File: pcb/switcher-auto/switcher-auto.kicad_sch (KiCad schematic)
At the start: 24 parts, among them J0 MD-90SM, J5 Conn_02x22_Top_Bottom, SW1 SW_Push, SW2 SW_Push, U1 CD74HC4067SM96, U2 CD74HC4067SM96, U3 CD74HC4067SM96, U4 CD74HC4067SM96, U5 CD74HC4067SM96, U6 CD74HC4067SM96, U7 CD74HC4067SM96

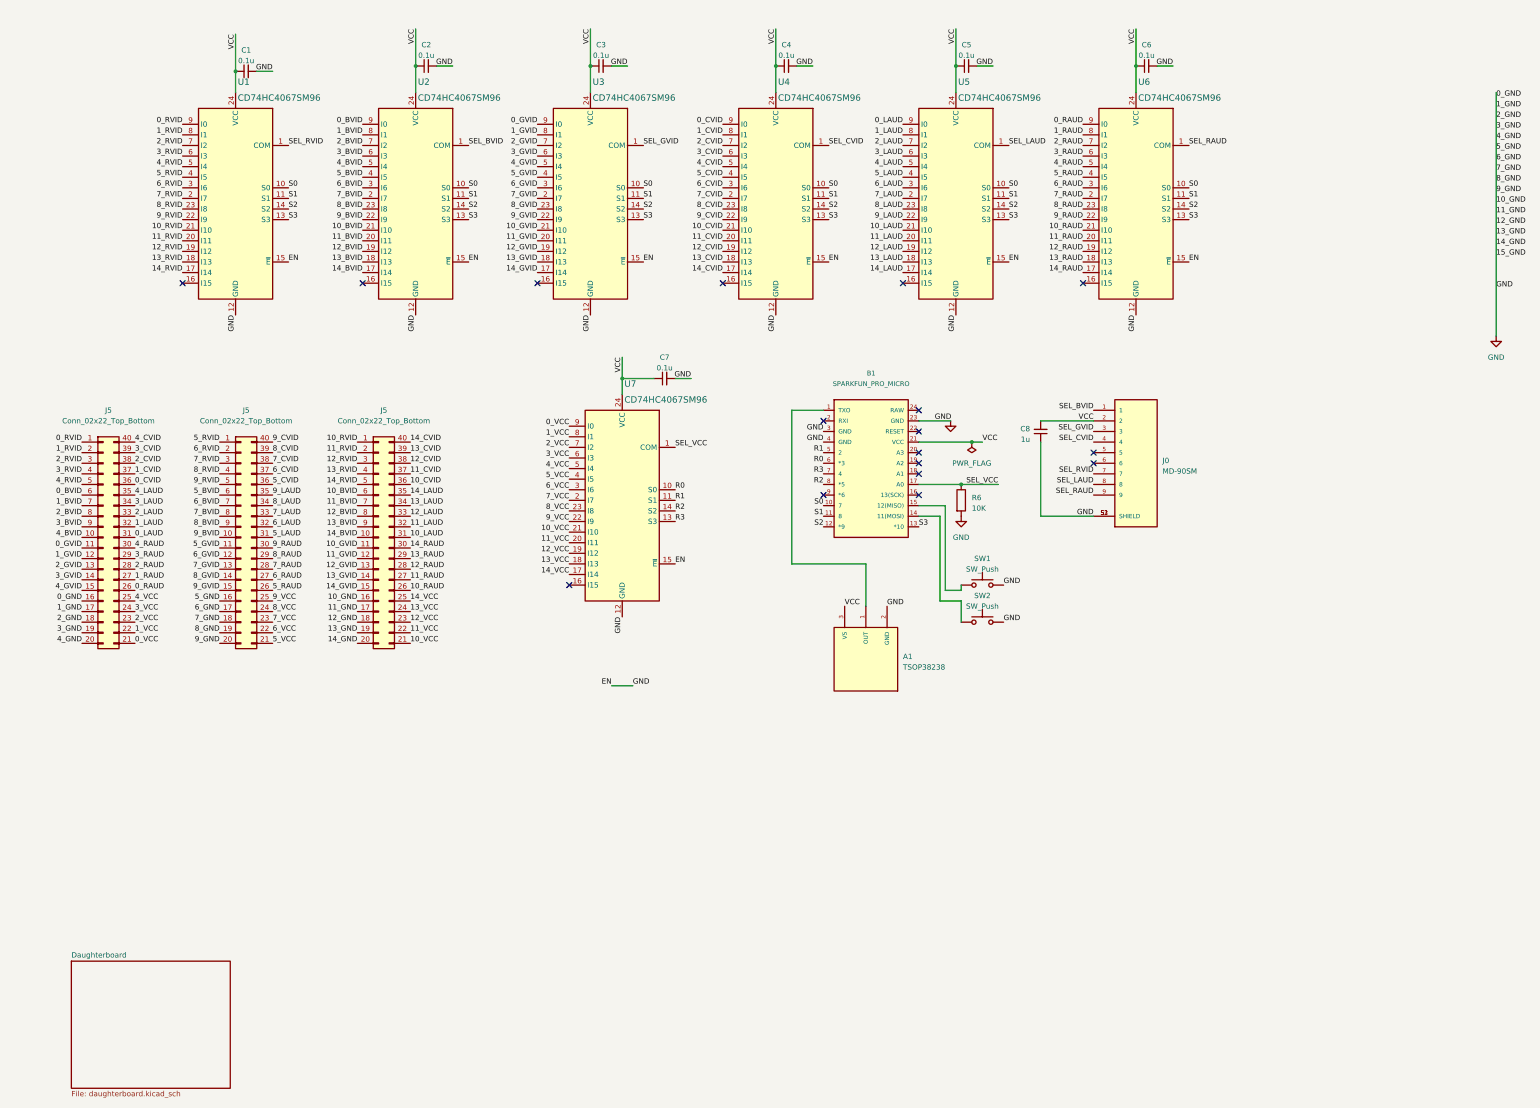
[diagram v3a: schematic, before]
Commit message: Adds THS7374 video amp
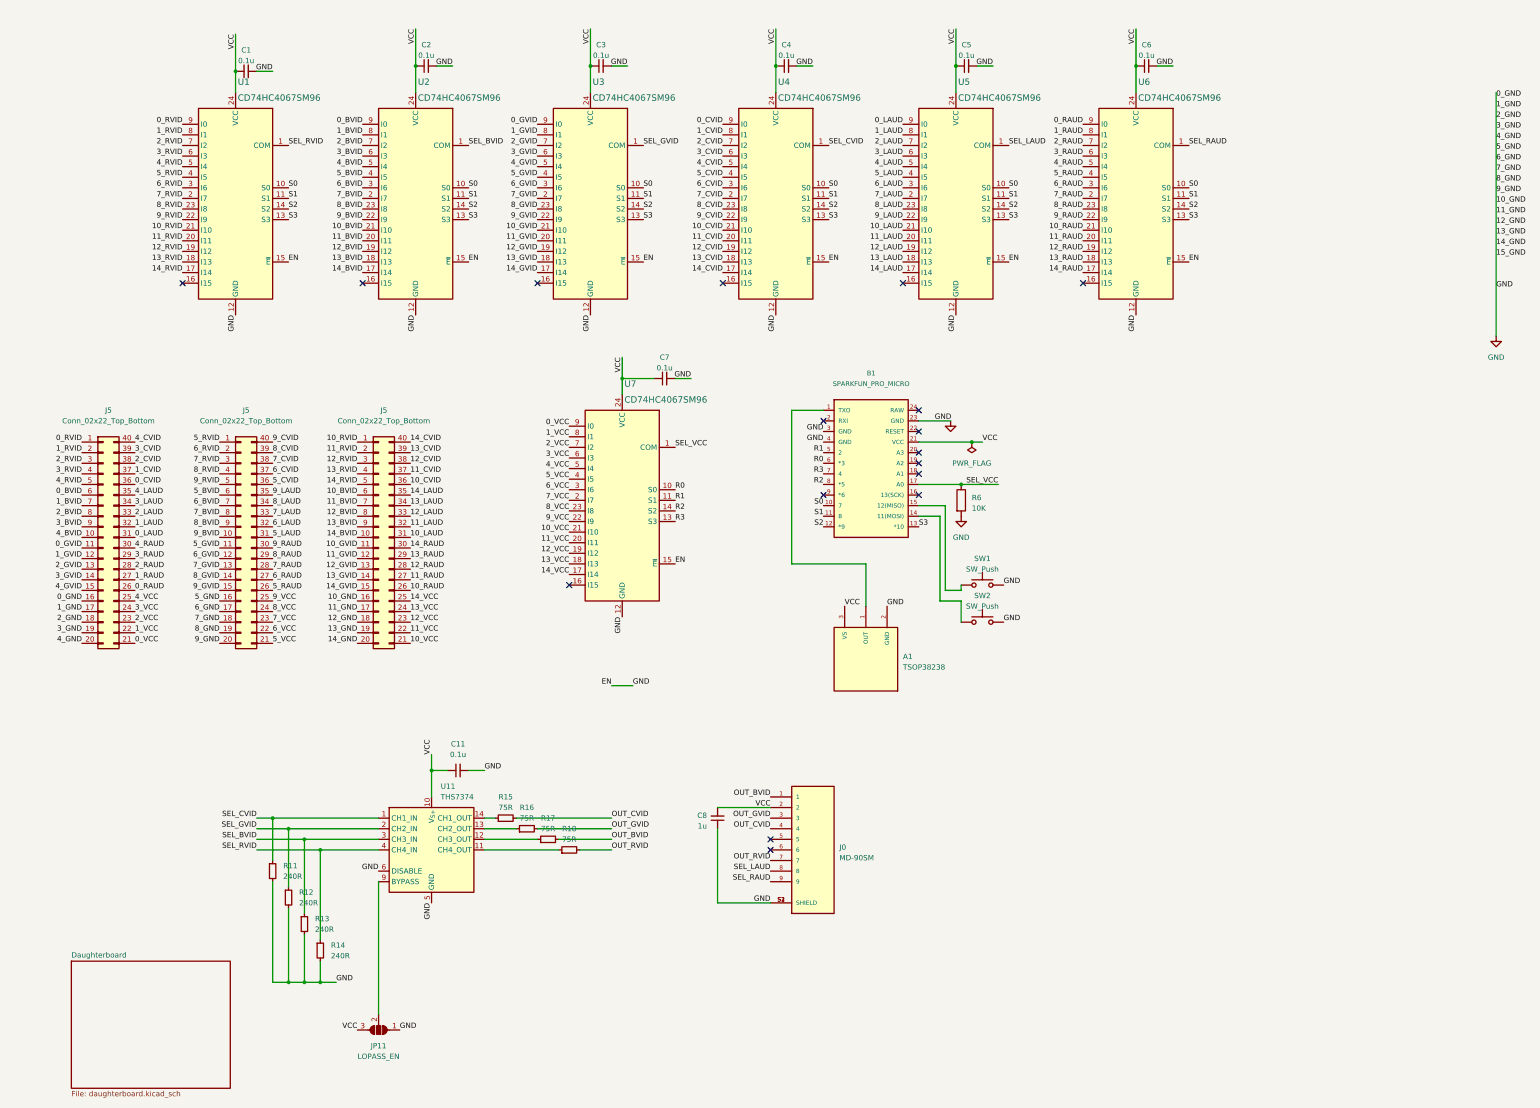
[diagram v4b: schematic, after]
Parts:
- added C11: 0.1u, Capacitor_SMD:C_0805_2012Metric_Pad1.18x1.45mm_HandSolder, symbol Device:C_Small
- added JP11: LOPASS_EN, Jumper:SolderJumper-3_P1.3mm_Open_RoundedPad1.0x1.5mm_NumberLabels, symbol Jumper:SolderJumper_3_Open
- added R11, R12, R13, R14: 240R, Resistor_SMD:R_0805_2012Metric_Pad1.20x1.40mm_HandSolder, symbol Device:R_Small
- added R15, R16, R17, R18: 75R, Resistor_SMD:R_0805_2012Metric_Pad1.20x1.40mm_HandSolder, symbol Device:R_Small
- added U11: THS7374, Package_SO:TSSOP-14_4.4x5mm_P0.65mm, symbol Amplifier_Video:THS7374
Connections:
- net GND: now also C11.2, JP11.1 (A), R11.2, R12.2, R13.2, R14.2, U11.5 (GND), U11.6 (DISABLE)
- net SEL_BVID: now also R13.1, U11.3 (CH3_IN); no longer J0.1
- net SEL_CVID: now also R11.1, U11.1 (CH1_IN); no longer J0.4
- net SEL_GVID: now also R12.1, U11.2 (CH2_IN); no longer J0.3
- net SEL_RVID: now also R14.1, U11.4 (CH4_IN); no longer J0.7
- net VCC: now also C11.1, JP11.3 (B), U11.10 (V_{S+})
- new net: R18.1, U11.11 (CH4_OUT)
- new net: R17.1, U11.12 (CH3_OUT)
- new net: R16.1, U11.13 (CH2_OUT)
- new net: R15.1, U11.14 (CH1_OUT)
- new net: JP11.2 (C), U11.9 (BYPASS)
- new net OUT_BVID: J0.1, R17.2
- new net OUT_CVID: J0.4, R15.2
- new net OUT_GVID: J0.3, R16.2
- new net OUT_RVID: J0.7, R18.2
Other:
- moved on the sheet: C8, J0

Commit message: Twiddles
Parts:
- added C12: C_Small, Capacitor_SMD:C_0805_2012Metric_Pad1.18x1.45mm_HandSolder, symbol Device:C_Small
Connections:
- net GND: now also C12.2
- net VCC: now also C12.1
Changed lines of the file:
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@@
   (junction (at 78.74 209.55) (diameter 0) (color 0 0 0 0)
   )
+  (junction (at 259.08 116.84) (diameter 0) (color 0 0 0 0)
+  )
   (junction (at 82.55 246.38) (diameter 0) (color 0 0 0 0)
   )
   (junction (at 238.76 26.67) (diameter 0) (color 0 0 0 0)
   )
-  (junction (at 242.57 116.84) (diameter 0) (color 0 0 0 0)
-  )
   (junction (at 86.36 246.38) (diameter 0) (color 0 0 0 0)
   )
@@
   (junction (at 86.36 214.63) (diameter 0) (color 0 0 0 0)
   )
+  (junction (at 248.92 116.84) (diameter 0) (color 0 0 0 0)
+  )
   (junction (at 113.03 195.58) (diameter 0) (color 0 0 0 0)
   )
@@
   )
   (junction (at 78.74 246.38) (diameter 0) (color 0 0 0 0)
-  )
-  (junction (at 240.03 127) (diameter 0) (color 0 0 0 0)
   )
   (junction (at 82.55 212.09) (diameter 0) (color 0 0 0 0)
@@
     (stroke (width 0) (type default))
   )
-  (wire (pts (xy 242.57 116.84) (xy 245.11 116.84))
-    (stroke (width 0) (type default))
-  )
   (wire (pts (xy 113.03 195.58) (xy 113.03 201.93))
     (stroke (width 0) (type default))
@@
     (stroke (width 0) (type default))
   )
+  (wire (pts (xy 248.92 116.84) (xy 259.08 116.84))
+    (stroke (width 0) (type default))
+  )
   (wire (pts (xy 71.12 209.55) (xy 78.74 209.55))
     (stroke (width 0) (type default))
@@
     (stroke (width 0) (type default))
   )
-  (wire (pts (xy 240.03 127) (xy 248.92 127))
-    (stroke (width 0) (type default))
-  )
   (wire (pts (xy 234.95 134.62) (xy 229.87 134.62))
     (stroke (width 0) (type default))
@@
     (stroke (width 0) (type default))
   )
-  (wire (pts (xy 229.87 116.84) (xy 242.57 116.84))
+  (wire (pts (xy 229.87 116.84) (xy 248.92 116.84))
     (stroke (width 0) (type default))
   )
@@
     (stroke (width 0) (type default))
   )
+  (wire (pts (xy 259.08 116.84) (xy 261.62 116.84))
+    (stroke (width 0) (type default))
+  )
   (wire (pts (xy 207.01 109.22) (xy 199.39 109.22))
     (stroke (width 0) (type default))
@@
     (effects (font (size 1.27 1.27)) (justify right bottom))
   )
-  (label "SEL_VCC" (at 248.92 127 180) (fields_autoplaced)
+  (label "SEL_VCC" (at 238.76 127 180) (fields_autoplaced)
     (effects (font (size 1.27 1.27)) (justify right bottom))
   )
@@
     (effects (font (size 1.27 1.27)) (justify left bottom))
   )
-  (label "VCC" (at 245.11 116.84 0) (fields_autoplaced)
+  (label "VCC" (at 261.62 116.84 0) (fields_autoplaced)
     (effects (font (size 1.27 1.27)) (justify left bottom))
   )
@@
     )
   )
+  (symbol (lib_id "power:GND") (at 248.92 121.92 0) (unit 1)
+    (in_bom yes) (on_board yes) (dnp no) (fields_autoplaced)
+    (property "Reference" "#PWR011" (at 248.92 128.27 0)
+      (effects (font (size 1.27 1.27)) hide)
+    )
+    (property "Value" "GND" (at 248.92 127 0)
+      (effects (font (size 1.27 1.27)))
+    )
+    (property "Footprint" "" (at 248.92 121.92 0)
+      (effects (font (size 1.27 1.27)) hide)
+    )
+    (property "Datasheet" "" (at 248.92 121.92 0)
+      (effects (font (size 1.27 1.27)) hide)
+    )
+    (pin "1")
+    (instances
+      (project "switcher-auto"
+        (path "/e72d49f3-4a7e-4284-a905-90a44014e1f4"
+          (reference "#PWR011") (unit 1)
+        )
+      )
+    )
+  )
   (symbol (lib_id "power:GND") (at 368.3 91.44 0) (unit 1)
     (in_bom yes) (on_board yes) (dnp no) (fields_autoplaced)
@@
     )
   )
-  (symbol (lib_id "power:PWR_FLAG") (at 242.57 116.84 180) (unit 1)
+  (symbol (lib_id "power:PWR_FLAG") (at 259.08 116.84 0) (unit 1)
     (in_bom yes) (on_board yes) (dnp no) (fields_autoplaced)
-    (property "Reference" "#FLG01" (at 242.57 118.745 0)
-      (effects (font (size 1.27 1.27)) hide)
-    )
-    (property "Value" "PWR_FLAG" (at 242.57 121.92 0)
-      (effects (font (size 1.27 1.27)))
-    )
-    (property "Footprint" "" (at 242.57 116.84 0)
-      (effects (font (size 1.27 1.27)) hide)
-    )
-    (property "Datasheet" "~" (at 242.57 116.84 0)
+    (property "Reference" "#FLG01" (at 259.08 114.935 0)
+      (effects (font (size 1.27 1.27)) hide)
+    )
+    (property "Value" "PWR_FLAG" (at 259.08 111.76 0)
+      (effects (font (size 1.27 1.27)))
+    )
+    (property "Footprint" "" (at 259.08 116.84 0)
+      (effects (font (size 1.27 1.27)) hide)
+    )
+    (property "Datasheet" "~" (at 259.08 116.84 0)
       (effects (font (size 1.27 1.27)) hide)
     )
@@
         )
       )
+    )
+  )
+  (symbol (lib_id "Device:C_Small") (at 248.92 119.38 0) (unit 1)
+    (in_bom yes) (on_board yes) (dnp no) (fields_autoplaced)
+    (property "Reference" "C12" (at 251.46 118.1163 0)
+      (effects (font (size 1.27 1.27)) (justify left))
+    )
+    (property "Value" "C_Small" (at 251.46 120.6563 0)
+      (effects (font (size 1.27 1.27)) (justify left))
+    )
+    (property "Footprint" "Capacitor_SMD:C_0805_2012Metric_Pad1.18x1.45mm_HandSolder" (at 248.92 119.38 0)
+      (effects (font (size 1.27 1.27)) hide)
+    )
+    (property "Datasheet" "~" (at 248.92 119.38 0)
+      (effects (font (size 1.27 1.27)) hide)
+    )
+    (pin "1")
+    (pin "2")
+    (instances
+      (project "switcher-auto"
+        (path "/e72d49f3-4a7e-4284-a905-90a44014e1f4"
+          (reference "C12") (unit 1)
+        )
+      )
